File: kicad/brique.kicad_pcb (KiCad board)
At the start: 4 copper layers, 42.1 x 107.7 mm, 126 parts, among them J1 Conn_01x07, J2 USB_B_Micro, J3 Speaker Pads, J4 Battery Connection Pads, J6 SM03B-SRSS-TB, J7 SM03B-SRSS-TB, M1 Vibration, Q1 BC847, Q2 BC847, Q3 BC847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

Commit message: Fix part numbers
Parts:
- C11, C12, C13, C14, C15, C16, C17, C18, C2, C20, C21, C25, C5, C8: value 100n -> 100nF
- J6, J7: value SM03B-SRSS-TB -> BM03B-SRSS-TB
- L3: value ~ -> BLM18EG471SN1D
- moved C12 1.53 mm to (50.5, 60.5)
- moved L3 0.23 mm to (47.8, 21.0)
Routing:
- net +3V3: track 188.4 -> 189.5 mm
- net GND: track 245.4 -> 244.7 mm
- net QSPI_SCLK: track 15.7 -> 14.9 mm

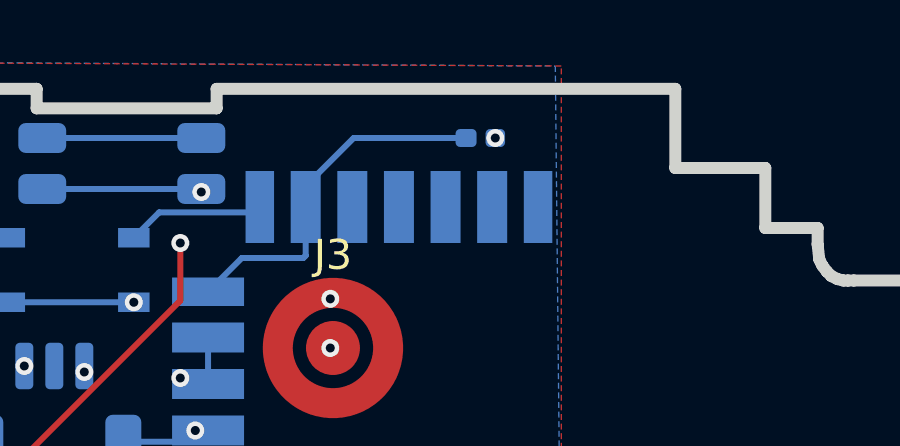
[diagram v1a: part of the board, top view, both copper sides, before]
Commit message: fix bad footprints
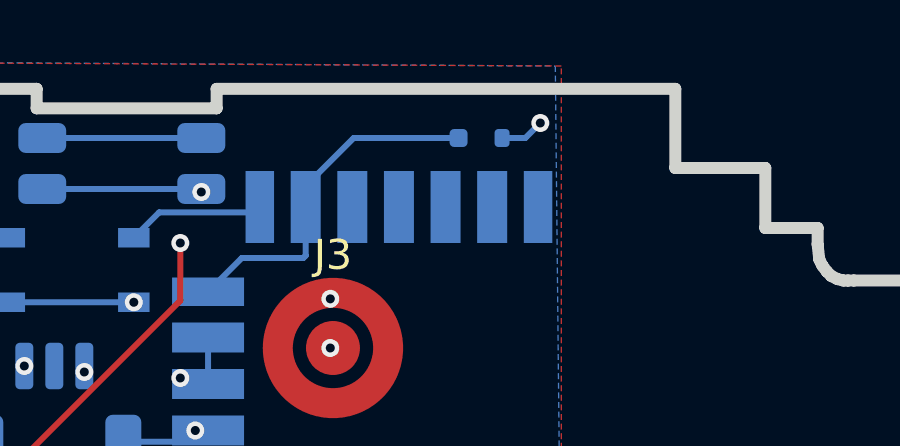
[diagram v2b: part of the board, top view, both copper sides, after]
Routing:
- net +3V3: track 189.5 -> 191.0 mm
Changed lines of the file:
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@@
 			)
 		)
-		(property "JLCPCB" "C171589"
+		(property "JLCPCB" "C57269"
 			(at 0 0 0)
 			(unlocked yes)
@@
 		(tags "inductor")
 		(property "Reference" "L3"
-			(at -1.655 0.6 0)
+			(at -1.655 0.1 0)
 			(layer "B.SilkS")
 			(effects
@@
 		)
 		(pad "1" smd roundrect
-			(at -0.225 0 180)
-			(size 0.65 0.6)
+			(at -0.45 0 180)
+			(size 0.5 0.6)
 			(layers "B.Cu" "B.Mask")
 			(roundrect_rratio 0.25)
@@
 		)
 		(pad "2" smd roundrect
-			(at 0.75 0 180)
-			(size 0.7 0.6)
+			(at 1 0 180)
+			(size 0.6 0.6)
 			(layers "B.Cu" "B.Mask")
 			(roundrect_rratio 0.25)
@@
 	)
 	(via
-		(at 48 21)
+		(at 49.5 20.5)
 		(size 0.6)
 		(drill 0.3)
@@
 	)
 	(segment
+		(start 48.225 21)
+		(end 49 21)
+		(width 0.2)
+		(layer "B.Cu")
+		(net 6)
+	)
+	(segment
 		(start 61.605 94.335001)
 		(end 61.605 95.49)
@@
 	)
 	(segment
+		(start 49 21)
+		(end 49.5 20.5)
+		(width 0.2)
+		(layer "B.Cu")
+		(net 6)
+	)
+	(segment
 		(start 49.05 86.05)
 		(end 44.6 86.05)
@@
 	)
 	(segment
-		(start 41.67917 23.3)
-		(end 41.67917 22.6)
+		(start 38.425 26.125)
+		(end 39.55 25)
 		(width 0.2)
 		(layer "B.Cu")
@@
 	)
 	(segment
-		(start 38.425 26.125)
-		(end 39.55 25)
+		(start 41.67917 23.3)
+		(end 41.67917 22.6)
 		(width 0.2)
 		(layer "B.Cu")
@@
 	(segment
 		(start 43.27917 21)
-		(end 47.025 21)
+		(end 46.775 21)
 		(width 0.2)
 		(layer "B.Cu")
